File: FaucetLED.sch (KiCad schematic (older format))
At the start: 41 parts, among them P1 CONN_01X03, P2 CONN_01X02, P3 CONN_01X01, P4 CONN_01X03, P5 CONN_01X02, P6 CONN_01X01, Q1 BSS138, Q2 BSS138, Q3 BSS138, U1 TLV70033DDC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

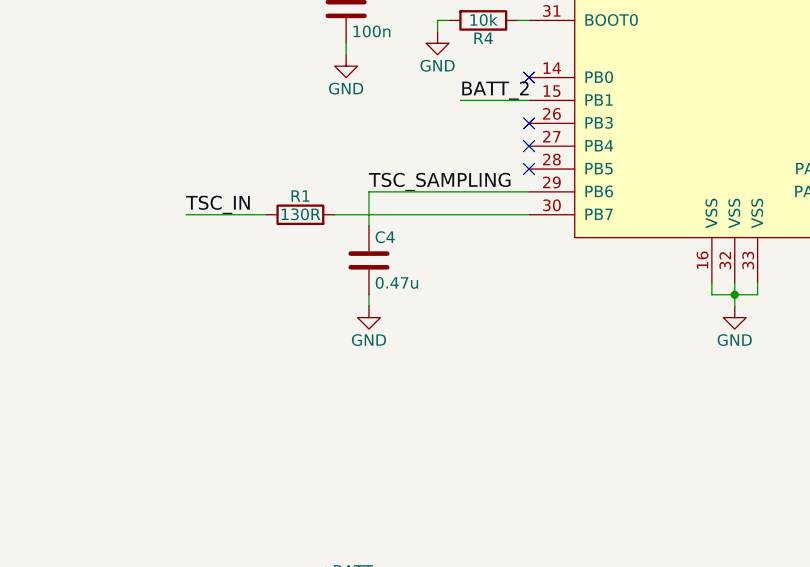
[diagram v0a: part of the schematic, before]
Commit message: C4: Sampling capacitor: Change value to 0.1uF.
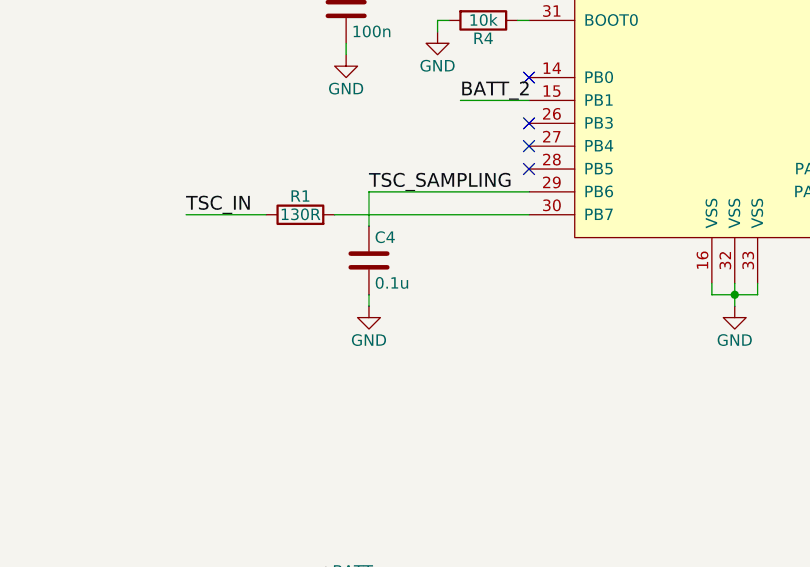
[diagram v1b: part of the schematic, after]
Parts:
- C4: value 0.47u -> 0.1u
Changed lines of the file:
@@
 P 4050 4200
 F 0 "C4" H 4075 4300 50  0000 L CNN
-F 1 "0.47u" H 4075 4100 50  0000 L CNN
+F 1 "0.1u" H 4075 4100 50  0000 L CNN
 F 2 "components:C_0603_0805" H 4088 4050 50  0001 C CNN
 F 3 "" H 4050 4200 50  0000 C CNN

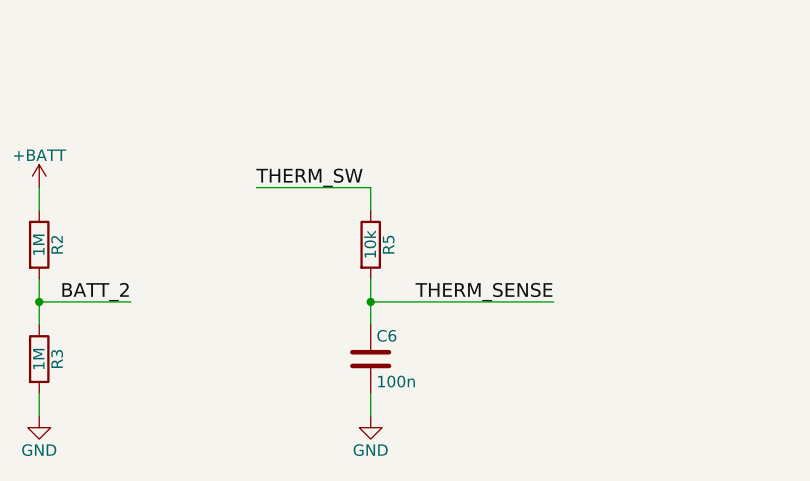
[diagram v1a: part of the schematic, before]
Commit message: Fix THERM_SENSE topology to form proper voltage divider.
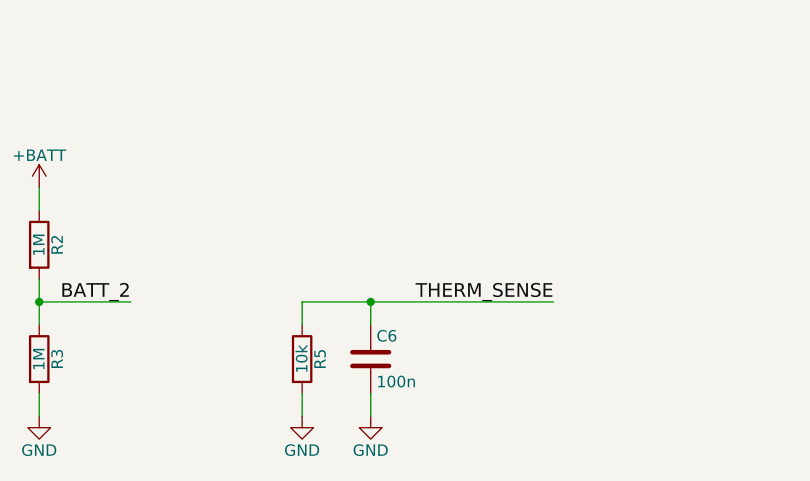
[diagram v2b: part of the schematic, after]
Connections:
- net GND: now also R5.2
- net THERM_SENSE: now also R5.1; no longer R5.2
- net THERM_SW: no longer R5.1
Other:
- moved on the sheet: R5
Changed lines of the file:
@@
 L R R5
 U 1 1 5855D75A
-P 5400 5950
-F 0 "R5" V 5480 5950 50  0000 C CNN
-F 1 "10k" V 5400 5950 50  0000 C CNN
-F 2 "components:R_0603_0805" V 5330 5950 50  0001 C CNN
-F 3 "" H 5400 5950 50  0000 C CNN
-	1    5400 5950
+P 5100 6450
+F 0 "R5" V 5180 6450 50  0000 C CNN
+F 1 "10k" V 5100 6450 50  0000 C CNN
+F 2 "components:R_0603_0805" V 5030 6450 50  0001 C CNN
+F 3 "" H 5100 6450 50  0000 C CNN
+	1    5100 6450
 	1    0    0    -1
 $EndComp
@@
 	1    0    0    -1
 $EndComp
-Text Label 4900 5700 0    60   ~ 0
-THERM_SW
 $Comp
 L C C6
@@
 	3950 6600 3950 6700
 Wire Wire Line
-	5400 6200 6200 6200
-Wire Wire Line
-	4900 5700 5400 5700
-Wire Wire Line
-	5400 5700 5400 5800
+	5100 6200 6200 6200
 Wire Wire Line
 	5400 6600 5400 6700
@@
 Wire Wire Line
 	3600 4000 3250 4000
-Wire Wire Line
-	5400 6100 5400 6300
 NoConn ~ 4750 3400
 NoConn ~ 4750 3600
@@
 Wire Wire Line
 	1550 6300 1550 6250
+$Comp
+L GND #PWR?
+U 1 1 58BF6470
+P 5100 6700
+F 0 "#PWR?" H 5100 6450 50  0001 C CNN
+F 1 "GND" H 5100 6550 50  0000 C CNN
+F 2 "" H 5100 6700 50  0000 C CNN
+F 3 "" H 5100 6700 50  0000 C CNN
+	1    5100 6700
+	1    0    0    -1
+$EndComp
+Wire Wire Line
+	5100 6700 5100 6600
+Wire Wire Line
+	5100 6300 5100 6200
+Wire Wire Line
+	5400 6300 5400 6200
 $EndSCHEMATC

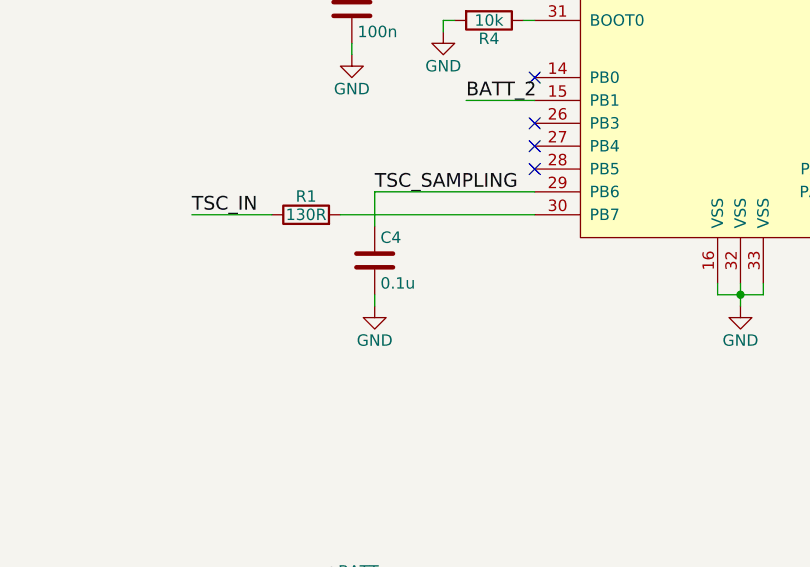
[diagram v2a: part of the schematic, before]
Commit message: C4: Change sampling capacitor to 47nF.
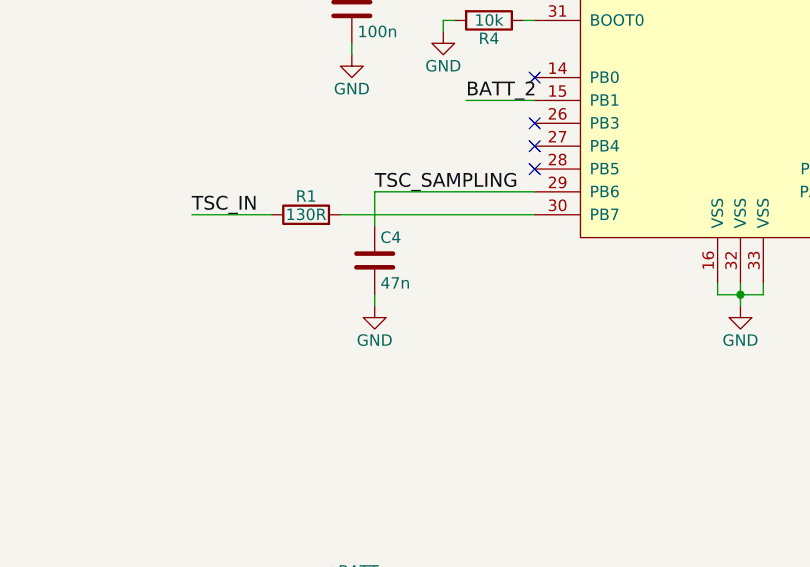
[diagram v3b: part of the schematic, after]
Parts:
- C4: value 0.1u -> 47n
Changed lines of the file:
@@
 P 4050 4200
 F 0 "C4" H 4075 4300 50  0000 L CNN
-F 1 "0.1u" H 4075 4100 50  0000 L CNN
+F 1 "47n" H 4075 4100 50  0000 L CNN
 F 2 "components:C_0603_0805" H 4088 4050 50  0001 C CNN
 F 3 "" H 4050 4200 50  0000 C CNN

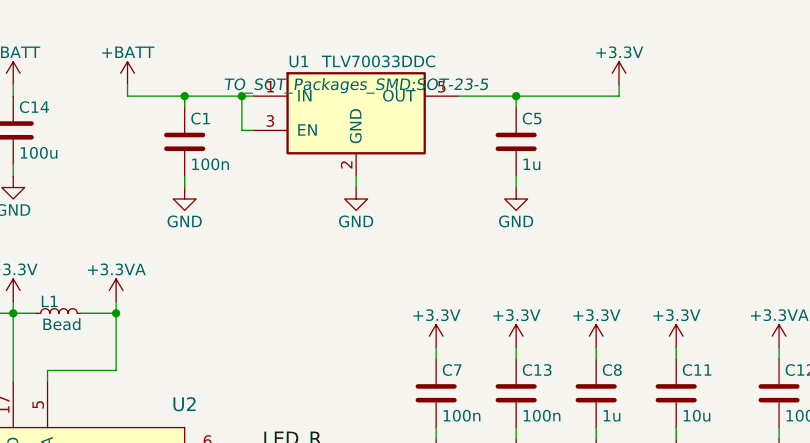
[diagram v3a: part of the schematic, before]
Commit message: U1: Change to TPS782 3.3V regulator for lower Iq.
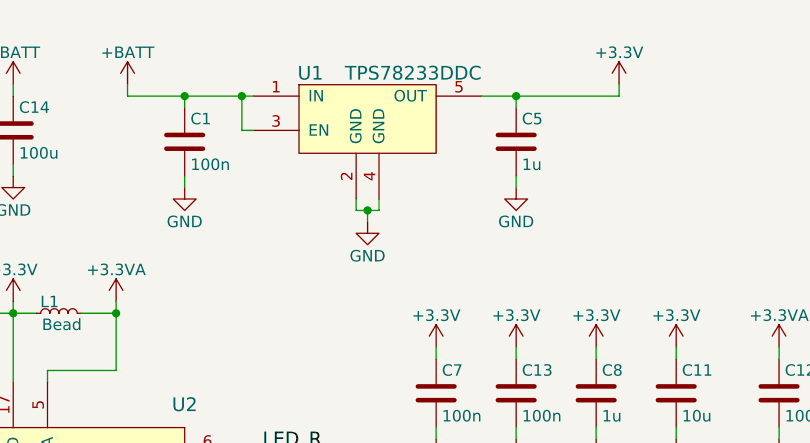
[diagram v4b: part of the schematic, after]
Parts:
- removed U1: TLV70033DDC, TO_SOT_Packages_SMD:SOT-23-5, symbol TLV70033DDC
- added U1: TPS78233DDC, symbol TPS78233DDC
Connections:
- net +3V3: now also U1.5 (OUT)
- net +BATT: now also U1.1 (IN), U1.3 (EN)
- net GND: now also U1.2 (GND), U1.4 (GND)
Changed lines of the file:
@@
 	3950 6100 3950 6300
-$Comp
-L TLV70033DDC U1
-U 1 1 58AAC1C2
-P 7150 1000
-F 0 "U1" H 6900 1200 50  0000 C CNN
-F 1 "TLV70033DDC" H 7250 1200 50  0000 C CNN
-F 2 "TO_SOT_Packages_SMD:SOT-23-5" H 7150 1100 50  0000 C CIN
-F 3 "" H 7150 1000 50  0000 C CNN
-F 4 "296-27937-1-ND" H 7150 1000 60  0001 C CNN "DigiKey PN"
-F 5 "TLV70033DDCR" H 7150 1000 60  0001 C CNN "Manufacturer PN"
-	1    7150 1000
-	1    0    0    -1
-$EndComp
 $Comp
 L C C5
@@
 	8300 900  8300 950
 Wire Wire Line
-	8300 950  7600 950
-Wire Wire Line
 	7850 1000 7850 950
 Connection ~ 7850 950
@@
 L GND #PWR016
 U 1 1 58AAC750
-P 7150 1350
-F 0 "#PWR016" H 7150 1100 50  0001 C CNN
-F 1 "GND" H 7150 1200 50  0000 C CNN
-F 2 "" H 7150 1350 50  0000 C CNN
-F 3 "" H 7150 1350 50  0000 C CNN
-	1    7150 1350
-	1    0    0    -1
-$EndComp
-Wire Wire Line
-	7150 1300 7150 1350
+P 7200 1500
+F 0 "#PWR016" H 7200 1250 50  0001 C CNN
+F 1 "GND" H 7200 1350 50  0000 C CNN
+F 2 "" H 7200 1500 50  0000 C CNN
+F 3 "" H 7200 1500 50  0000 C CNN
+	1    7200 1500
+	1    0    0    -1
+$EndComp
 Wire Wire Line
 	7850 1300 7850 1350
@@
 Wire Wire Line
 	5400 6300 5400 6200
+$Comp
+L TPS78233DDC U1
+U 1 1 58C87FA9
+P 7200 1150
+F 0 "U1" H 6950 1450 60  0000 C CNN
+F 1 "TPS78233DDC" H 7400 1450 60  0000 C CNN
+F 2 "" H 7150 1150 60  0001 C CNN
+F 3 "" H 7150 1150 60  0001 C CNN
+	1    7200 1150
+	1    0    0    -1
+$EndComp
+Wire Wire Line
+	7150 1400 7150 1450
+Wire Wire Line
+	7150 1450 7250 1450
+Wire Wire Line
+	7250 1450 7250 1400
+Wire Wire Line
+	7200 1500 7200 1450
+Connection ~ 7200 1450
+Wire Wire Line
+	8300 950  7700 950
 $EndSCHEMATC

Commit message: C11: Change footprint to 0603 since 1206 was unnecessary.
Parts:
- C11: footprint Capacitors_SMD:C_1206 -> Capacitors_SMD:C_0603; DigiKey PN (none) -> 587-1256-1-ND; Note DNP -> (none)
- U1: footprint (none) -> TO_SOT_Packages_SMD:SOT-23-5
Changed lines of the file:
@@
 F 0 "C11" H 8575 2350 50  0000 L CNN
 F 1 "10u" H 8575 2150 50  0000 L CNN
-F 2 "Capacitors_SMD:C_1206" H 8588 2100 50  0001 C CNN
+F 2 "Capacitors_SMD:C_0603" H 8588 2100 50  0001 C CNN
 F 3 "" H 8550 2250 50  0000 C CNN
-F 4 "DNP" H 8550 2250 60  0001 C CNN "Note"
+F 4 "587-1256-1-ND" H 8550 2250 60  0001 C CNN "DigiKey PN"
 	1    8550 2250
 	1    0    0    -1
@@
 	1550 6300 1550 6250
 $Comp
-L GND #PWR?
+L GND #PWR043
 U 1 1 58BF6470
 P 5100 6700
-F 0 "#PWR?" H 5100 6450 50  0001 C CNN
+F 0 "#PWR043" H 5100 6450 50  0001 C CNN
 F 1 "GND" H 5100 6550 50  0000 C CNN
 F 2 "" H 5100 6700 50  0000 C CNN
@@
 F 0 "U1" H 6950 1450 60  0000 C CNN
 F 1 "TPS78233DDC" H 7400 1450 60  0000 C CNN
-F 2 "" H 7150 1150 60  0001 C CNN
+F 2 "TO_SOT_Packages_SMD:SOT-23-5" H 7150 1150 60  0001 C CNN
 F 3 "" H 7150 1150 60  0001 C CNN
 	1    7200 1150

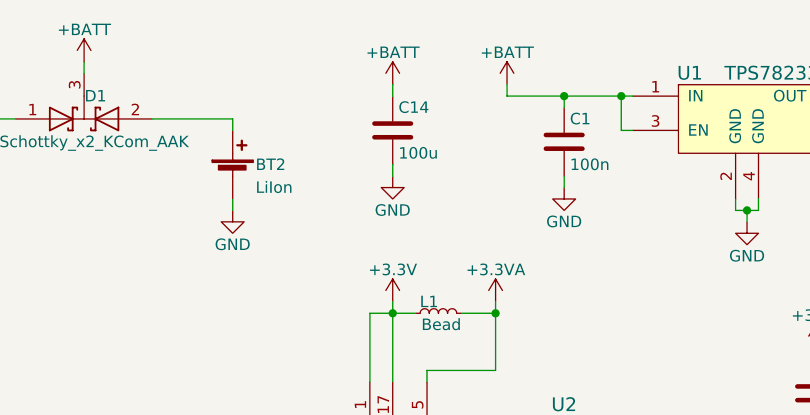
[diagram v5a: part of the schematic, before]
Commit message: Remove C14 (extra 100uF) since testing showed it was unnecessary.
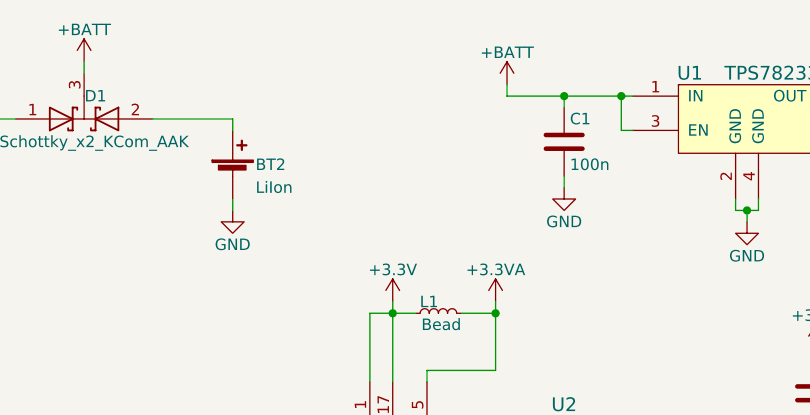
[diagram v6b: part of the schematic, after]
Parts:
- removed C14: 100u, Capacitors_SMD:C_1210, symbol C
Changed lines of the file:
@@
 Connection ~ 1900 1050
-$Comp
-L C C14
-U 1 1 58B28B0E
-P 5650 1100
-F 0 "C14" H 5675 1200 50  0000 L CNN
-F 1 "100u" H 5675 1000 50  0000 L CNN
-F 2 "Capacitors_SMD:C_1210" H 5688 950 50  0001 C CNN
-F 3 "" H 5650 1100 50  0000 C CNN
-F 4 "587-4313-1-ND" H 5650 1100 60  0001 C CNN "DigiKey PN"
-	1    5650 1100
-	1    0    0    -1
-$EndComp
-$Comp
-L +BATT #PWR040
-U 1 1 58B28BAB
-P 5650 900
-F 0 "#PWR040" H 5650 750 50  0001 C CNN
-F 1 "+BATT" H 5650 1040 50  0000 C CNN
-F 2 "" H 5650 900 50  0000 C CNN
-F 3 "" H 5650 900 50  0000 C CNN
-	1    5650 900
-	1    0    0    -1
-$EndComp
-Wire Wire Line
-	5650 900  5650 950
-$Comp
-L GND #PWR041
-U 1 1 58B28CDC
-P 5650 1300
-F 0 "#PWR041" H 5650 1050 50  0001 C CNN
-F 1 "GND" H 5650 1150 50  0000 C CNN
-F 2 "" H 5650 1300 50  0000 C CNN
-F 3 "" H 5650 1300 50  0000 C CNN
-	1    5650 1300
-	1    0    0    -1
-$EndComp
-Wire Wire Line
-	5650 1250 5650 1300
 $Comp
 L CONN_01X01 P3

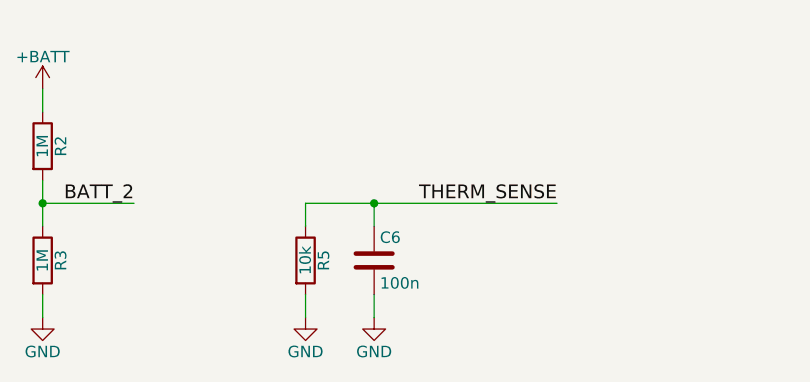
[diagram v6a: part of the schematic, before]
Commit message: C6: Change to 1uF for <50/60Hz cutoff freq.
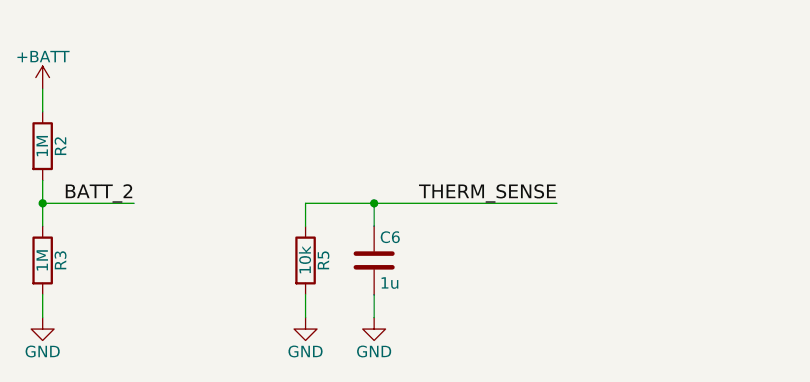
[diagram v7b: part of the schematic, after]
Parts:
- C6: value 100n -> 1u
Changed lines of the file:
@@
 P 5400 6450
 F 0 "C6" H 5425 6550 50  0000 L CNN
-F 1 "100n" H 5425 6350 50  0000 L CNN
+F 1 "1u" H 5425 6350 50  0000 L CNN
 F 2 "components:C_0603_0805" H 5438 6300 50  0001 C CNN
 F 3 "" H 5400 6450 50  0000 C CNN

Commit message: U1: Add Digikey PN.
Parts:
- U1: DigiKey PN (none) -> 296-24059-1-ND
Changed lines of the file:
@@
 $EndComp
 $Comp
-L +3.3V #PWR042
+L +3.3V #PWR040
 U 1 1 58B360F5
 P 1550 6250
-F 0 "#PWR042" H 1550 6100 50  0001 C CNN
+F 0 "#PWR040" H 1550 6100 50  0001 C CNN
 F 1 "+3.3V" H 1550 6390 50  0000 C CNN
 F 2 "" H 1550 6250 50  0000 C CNN
@@
 	1550 6300 1550 6250
 $Comp
-L GND #PWR043
+L GND #PWR041
 U 1 1 58BF6470
 P 5100 6700
-F 0 "#PWR043" H 5100 6450 50  0001 C CNN
+F 0 "#PWR041" H 5100 6450 50  0001 C CNN
 F 1 "GND" H 5100 6550 50  0000 C CNN
 F 2 "" H 5100 6700 50  0000 C CNN
@@
 F 2 "TO_SOT_Packages_SMD:SOT-23-5" H 7150 1150 60  0001 C CNN
 F 3 "" H 7150 1150 60  0001 C CNN
+F 4 "296-24059-1-ND" H 7200 1150 60  0001 C CNN "DigiKey PN"
 	1    7200 1150
 	1    0    0    -1
